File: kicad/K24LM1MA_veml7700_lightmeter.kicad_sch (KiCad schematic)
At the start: 45 parts, among them J1 Conn_01x08_Socket, J2 Conn_01x08_Socket, J3 Conn_01x04_Socket, J4 Conn_01x04_Socket, J5 USB_C_Receptacle_USB2.0 USB41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, Q1 DMG3402L, Q2 DMG3402L, SW1 SW_Push, SW2 SW_Push, SW3 SW_Push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

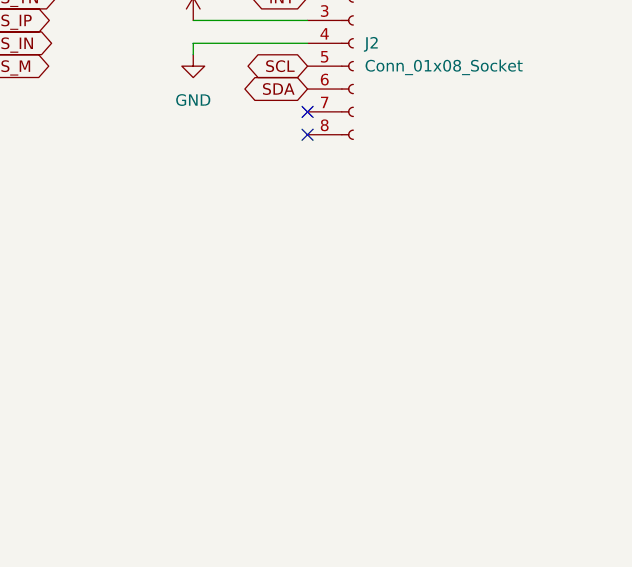
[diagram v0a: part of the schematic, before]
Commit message: layout components, switches changed to smd
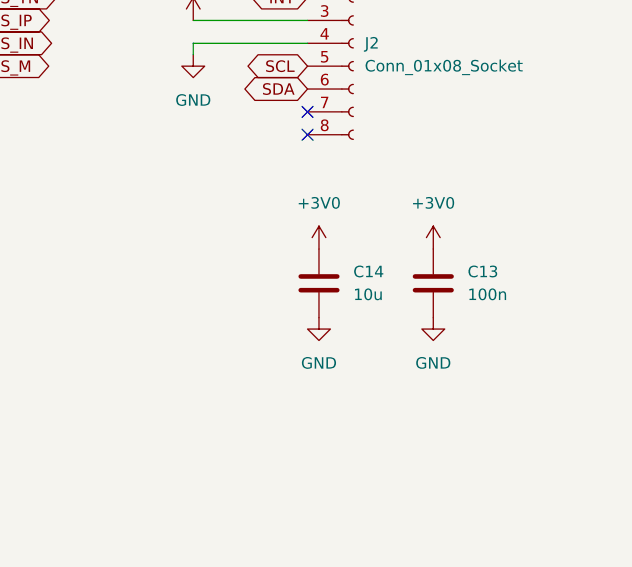
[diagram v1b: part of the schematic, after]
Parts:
- added C13: 100n, Capacitor_SMD:C_0603_1608Metric, symbol Device:C
- added C14: 10u, Capacitor_SMD:C_0603_1608Metric, symbol Device:C
- SW1, SW2, SW3, SW4, SW5: footprint Button_Switch_THT:SW_PUSH_6mm_H5mm -> Button_Switch_SMD:SW_Push_1P1T_NO_CK_KSC7xxJ
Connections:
- net +3V0: now also C13.2, C14.2
- net GND: now also C13.1, C14.1
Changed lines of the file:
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@@
       (effects (font (size 1.27 1.27)))
     )
-    (property "Footprint" "Button_Switch_THT:SW_PUSH_6mm_H5mm" (at 44.45 143.51 0)
+    (property "Footprint" "Button_Switch_SMD:SW_Push_1P1T_NO_CK_KSC7xxJ" (at 44.45 143.51 0)
       (effects (font (size 1.27 1.27)) hide)
     )
@@
     )
   )
+  (symbol (lib_id "power:GND") (at 259.08 67.31 0) (unit 1)
+    (in_bom yes) (on_board yes) (dnp no) (fields_autoplaced)
+    (property "Reference" "#PWR034" (at 259.08 73.66 0)
+      (effects (font (size 1.27 1.27)) hide)
+    )
+    (property "Value" "GND" (at 259.08 72.39 0)
+      (effects (font (size 1.27 1.27)))
+    )
+    (property "Footprint" "" (at 259.08 67.31 0)
+      (effects (font (size 1.27 1.27)) hide)
+    )
+    (property "Datasheet" "" (at 259.08 67.31 0)
+      (effects (font (size 1.27 1.27)) hide)
+    )
+    (pin "1")
+    (instances
+      (project "K24LM1MA_veml7700_lightmeter"
+        (path "/483fa7df-1bb3-4a22-bcb7-9bdf911b27cf"
+          (reference "#PWR034") (unit 1)
+        )
+      )
+    )
+  )
   (symbol (lib_id "power:+5V") (at 95.25 21.59 0) (unit 1)
     (in_bom yes) (on_board yes) (dnp no) (fields_autoplaced)
@@
       (effects (font (size 1.27 1.27)))
     )
-    (property "Footprint" "Button_Switch_THT:SW_PUSH_6mm_H5mm" (at 44.45 100.33 0)
+    (property "Footprint" "Button_Switch_SMD:SW_Push_1P1T_NO_CK_KSC7xxJ" (at 44.45 100.33 0)
       (effects (font (size 1.27 1.27)) hide)
     )
@@
       (effects (font (size 1.27 1.27)))
     )
-    (property "Footprint" "Button_Switch_THT:SW_PUSH_6mm_H5mm" (at 44.45 57.15 0)
+    (property "Footprint" "Button_Switch_SMD:SW_Push_1P1T_NO_CK_KSC7xxJ" (at 44.45 57.15 0)
       (effects (font (size 1.27 1.27)) hide)
     )
@@
       (effects (font (size 1.27 1.27)))
     )
-    (property "Footprint" "Button_Switch_THT:SW_PUSH_6mm_H5mm" (at 44.45 78.74 0)
+    (property "Footprint" "Button_Switch_SMD:SW_Push_1P1T_NO_CK_KSC7xxJ" (at 44.45 78.74 0)
       (effects (font (size 1.27 1.27)) hide)
     )
@@
         (path "/483fa7df-1bb3-4a22-bcb7-9bdf911b27cf"
           (reference "D4") (unit 1)
+        )
+      )
+    )
+  )
+  (symbol (lib_id "Device:C") (at 259.08 63.5 180) (unit 1)
+    (in_bom yes) (on_board yes) (dnp no) (fields_autoplaced)
+    (property "Reference" "C13" (at 262.89 62.23 0)
+      (effects (font (size 1.27 1.27)) (justify right))
+    )
+    (property "Value" "100n" (at 262.89 64.77 0)
+      (effects (font (size 1.27 1.27)) (justify right))
+    )
+    (property "Footprint" "Capacitor_SMD:C_0603_1608Metric" (at 258.1148 59.69 0)
+      (effects (font (size 1.27 1.27)) hide)
+    )
+    (property "Datasheet" "~" (at 259.08 63.5 0)
+      (effects (font (size 1.27 1.27)) hide)
+    )
+    (pin "2")
+    (pin "1")
+    (instances
+      (project "K24LM1MA_veml7700_lightmeter"
+        (path "/483fa7df-1bb3-4a22-bcb7-9bdf911b27cf"
+          (reference "C13") (unit 1)
         )
       )
@@
     )
   )
+  (symbol (lib_id "Device:C") (at 246.38 63.5 180) (unit 1)
+    (in_bom yes) (on_board yes) (dnp no) (fields_autoplaced)
+    (property "Reference" "C14" (at 250.19 62.23 0)
+      (effects (font (size 1.27 1.27)) (justify right))
+    )
+    (property "Value" "10u" (at 250.19 64.77 0)
+      (effects (font (size 1.27 1.27)) (justify right))
+    )
+    (property "Footprint" "Capacitor_SMD:C_0603_1608Metric" (at 245.4148 59.69 0)
+      (effects (font (size 1.27 1.27)) hide)
+    )
+    (property "Datasheet" "~" (at 246.38 63.5 0)
+      (effects (font (size 1.27 1.27)) hide)
+    )
+    (pin "2")
+    (pin "1")
+    (instances
+      (project "K24LM1MA_veml7700_lightmeter"
+        (path "/483fa7df-1bb3-4a22-bcb7-9bdf911b27cf"
+          (reference "C14") (unit 1)
+        )
+      )
+    )
+  )
   (symbol (lib_id "Device:LED") (at 116.84 25.4 90) (unit 1)
     (in_bom yes) (on_board yes) (dnp no) (fields_autoplaced)
@@
         (path "/483fa7df-1bb3-4a22-bcb7-9bdf911b27cf"
           (reference "D5") (unit 1)
+        )
+      )
+    )
+  )
+  (symbol (lib_id "power:+3V0") (at 246.38 59.69 0) (unit 1)
+    (in_bom yes) (on_board yes) (dnp no) (fields_autoplaced)
+    (property "Reference" "#PWR035" (at 246.38 63.5 0)
+      (effects (font (size 1.27 1.27)) hide)
+    )
+    (property "Value" "+3V0" (at 246.38 54.61 0)
+      (effects (font (size 1.27 1.27)))
+    )
+    (property "Footprint" "" (at 246.38 59.69 0)
+      (effects (font (size 1.27 1.27)) hide)
+    )
+    (property "Datasheet" "" (at 246.38 59.69 0)
+      (effects (font (size 1.27 1.27)) hide)
+    )
+    (pin "1")
+    (instances
+      (project "K24LM1MA_veml7700_lightmeter"
+        (path "/483fa7df-1bb3-4a22-bcb7-9bdf911b27cf"
+          (reference "#PWR035") (unit 1)
         )
       )
@@
     )
   )
+  (symbol (lib_id "power:+3V0") (at 259.08 59.69 0) (unit 1)
+    (in_bom yes) (on_board yes) (dnp no) (fields_autoplaced)
+    (property "Reference" "#PWR033" (at 259.08 63.5 0)
+      (effects (font (size 1.27 1.27)) hide)
+    )
+    (property "Value" "+3V0" (at 259.08 54.61 0)
+      (effects (font (size 1.27 1.27)))
+    )
+    (property "Footprint" "" (at 259.08 59.69 0)
+      (effects (font (size 1.27 1.27)) hide)
+    )
+    (property "Datasheet" "" (at 259.08 59.69 0)
+      (effects (font (size 1.27 1.27)) hide)
+    )
+    (pin "1")
+    (instances
+      (project "K24LM1MA_veml7700_lightmeter"
+        (path "/483fa7df-1bb3-4a22-bcb7-9bdf911b27cf"
+          (reference "#PWR033") (unit 1)
+        )
+      )
+    )
+  )
   (symbol (lib_id "power:GND") (at 149.86 40.64 0) (unit 1)
     (in_bom yes) (on_board yes) (dnp no) (fields_autoplaced)
@@
     )
   )
+  (symbol (lib_id "power:GND") (at 246.38 67.31 0) (unit 1)
+    (in_bom yes) (on_board yes) (dnp no) (fields_autoplaced)
+    (property "Reference" "#PWR036" (at 246.38 73.66 0)
+      (effects (font (size 1.27 1.27)) hide)
+    )
+    (property "Value" "GND" (at 246.38 72.39 0)
+      (effects (font (size 1.27 1.27)))
+    )
+    (property "Footprint" "" (at 246.38 67.31 0)
+      (effects (font (size 1.27 1.27)) hide)
+    )
+    (property "Datasheet" "" (at 246.38 67.31 0)
+      (effects (font (size 1.27 1.27)) hide)
+    )
+    (pin "1")
+    (instances
+      (project "K24LM1MA_veml7700_lightmeter"
+        (path "/483fa7df-1bb3-4a22-bcb7-9bdf911b27cf"
+          (reference "#PWR036") (unit 1)
+        )
+      )
+    )
+  )
   (symbol (lib_id "power:GND1") (at 59.69 90.17 0) (unit 1)
     (in_bom yes) (on_board yes) (dnp no) (fields_autoplaced)
@@
       (effects (font (size 1.27 1.27)))
     )
-    (property "Footprint" "Button_Switch_THT:SW_PUSH_6mm_H5mm" (at 44.45 121.92 0)
-      (effects (font (size 1.27 1.27)) hide)
-    )
+    (property "Footprint" "Button_Switch_SMD:SW_Push_1P1T_NO_CK_KSC7xxJ" (at 44.45 121.92 0)
+      (effects (font (size 1.27 1.27)) hide)
+    )
